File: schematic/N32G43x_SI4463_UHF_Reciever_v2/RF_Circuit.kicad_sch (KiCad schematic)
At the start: 93 parts, among them J1 U.FL, Q1 BC847BS, Q10 MMBT3904, Q11 MMBT3904, Q2 MMBT3904, Q3 BC847BS, Q4 BC847BS, Q5 BC847BS, Q6 BC847BS, Q7 BC847BS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

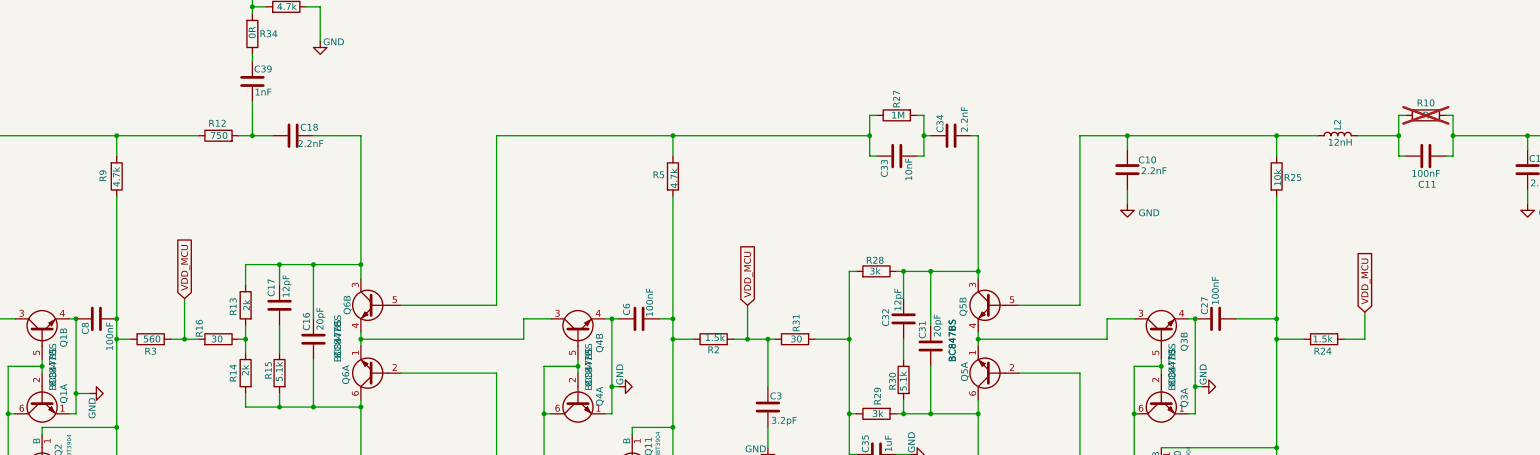
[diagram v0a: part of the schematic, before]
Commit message: Minor update to match pcb
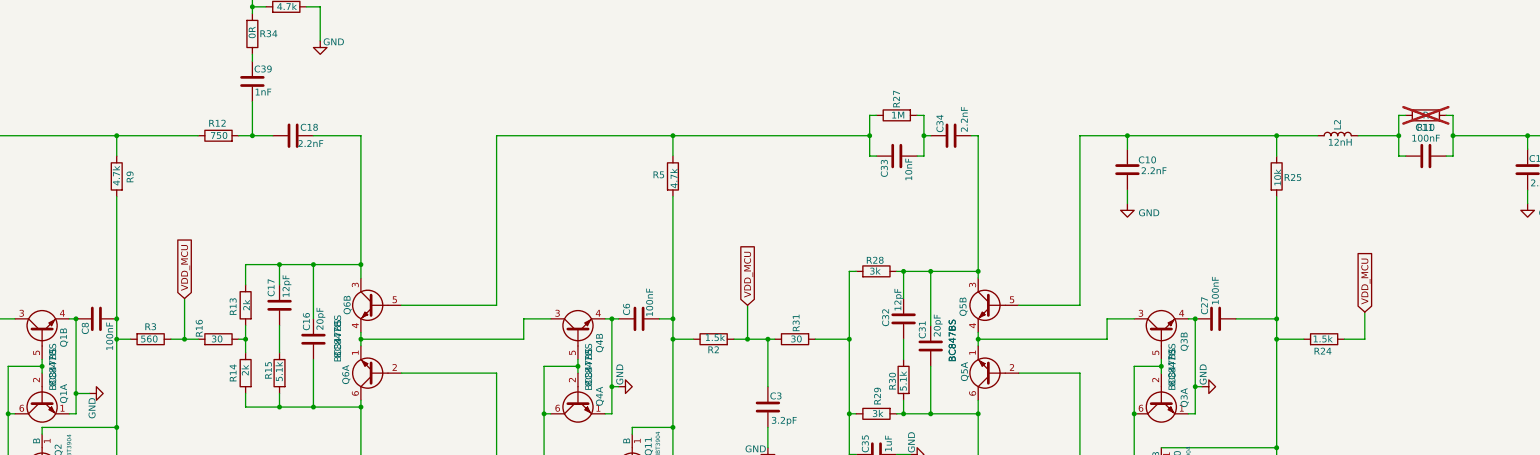
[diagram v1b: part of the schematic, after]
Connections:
- net VDD_MCU: now also R3.1; no longer R3.2
- net at C8.1, Q2.1 (B), Q2.3 (C)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: now also R3.2, R9.2; no longer R3.1, R9.1
- net at C12.2, D2.2, R6.1: now also C11.1, R10.2; no longer C11.2, R10.1
- net at Q7.5 (B2), R12.1: now also R9.1; no longer R9.2
- new net: C11.2, L2.2, R10.1
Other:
- moved on the sheet: C11, R10, R3
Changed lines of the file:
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@@
 	(symbol
 		(lib_id "Device:R")
-		(at 138.43 229.87 90)
+		(at 138.43 229.87 270)
 		(unit 1)
 		(exclude_from_sim no)
@@
 		(dnp no)
 		(property "Reference" "R3"
-			(at 138.43 232.156 90)
+			(at 138.43 227.584 90)
 			(effects
 				(font
@@
 		)
 		(property "Value" "560"
-			(at 138.684 229.87 90)
+			(at 138.176 229.87 90)
 			(effects
 				(font
@@
 		)
 		(property "Footprint" "Resistor_SMD:R_0805_2012Metric_Pad1.20x1.40mm_HandSolder"
-			(at 138.43 231.648 90)
+			(at 138.43 228.092 90)
 			(effects
 				(font
@@
 	(symbol
 		(lib_id "Device:R")
-		(at 377.19 187.96 270)
+		(at 377.19 187.96 90)
 		(unit 1)
 		(exclude_from_sim no)
@@
 		(dnp yes)
 		(property "Reference" "R10"
-			(at 377.19 185.674 90)
+			(at 377.19 190.246 90)
 			(effects
 				(font
@@
 		)
 		(property "Footprint" "Resistor_SMD:R_0805_2012Metric_Pad1.20x1.40mm_HandSolder"
-			(at 377.19 186.182 90)
+			(at 377.19 189.738 90)
 			(effects
 				(font
@@
 		(lib_id "Device:R")
 		(at 132.08 199.39 0)
-		(mirror x)
+		(mirror y)
 		(unit 1)
 		(exclude_from_sim no)
@@
 		(dnp no)
 		(property "Reference" "R9"
-			(at 129.54 198.12 90)
+			(at 134.62 200.66 90)
 			(effects
 				(font
@@
 		)
 		(property "Value" "4.7k"
-			(at 132.08 197.612 90)
+			(at 132.08 201.168 90)
 			(effects
 				(font
@@
 		)
 		(property "Footprint" "Resistor_SMD:R_0805_2012Metric_Pad1.20x1.40mm_HandSolder"
-			(at 130.302 199.39 90)
+			(at 133.858 199.39 90)
 			(effects
 				(font
@@
 	(symbol
 		(lib_id "Device:C")
-		(at 377.19 195.58 90)
+		(at 377.19 195.58 270)
 		(unit 1)
 		(exclude_from_sim no)
@@
 		(dnp no)
 		(property "Reference" "C11"
-			(at 377.444 200.914 90)
+			(at 376.936 190.246 90)
 			(effects
 				(font
@@
 		)
 		(property "Value" "100nF"
-			(at 377.19 198.882 90)
+			(at 377.19 192.278 90)
 			(effects
 				(font
@@
 		)
 		(property "Footprint" "Capacitor_SMD:C_0805_2012Metric_Pad1.18x1.45mm_HandSolder"
-			(at 381 194.6148 0)
-			(effects
-				(font
+			(at 373.38 196.5452 0)
+			(effects
+				(font
